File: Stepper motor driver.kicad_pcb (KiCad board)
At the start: 2 copper layers, 35.8 x 35.8 mm, 17 parts, among them P1 CONN_01X04, P2 CONN_01X03, P3 CONN_01X03, Q1 TIP120, Q2 TIP120, Q3 TIP120, Q4 TIP120, U1 74LS175, U2 74LS157

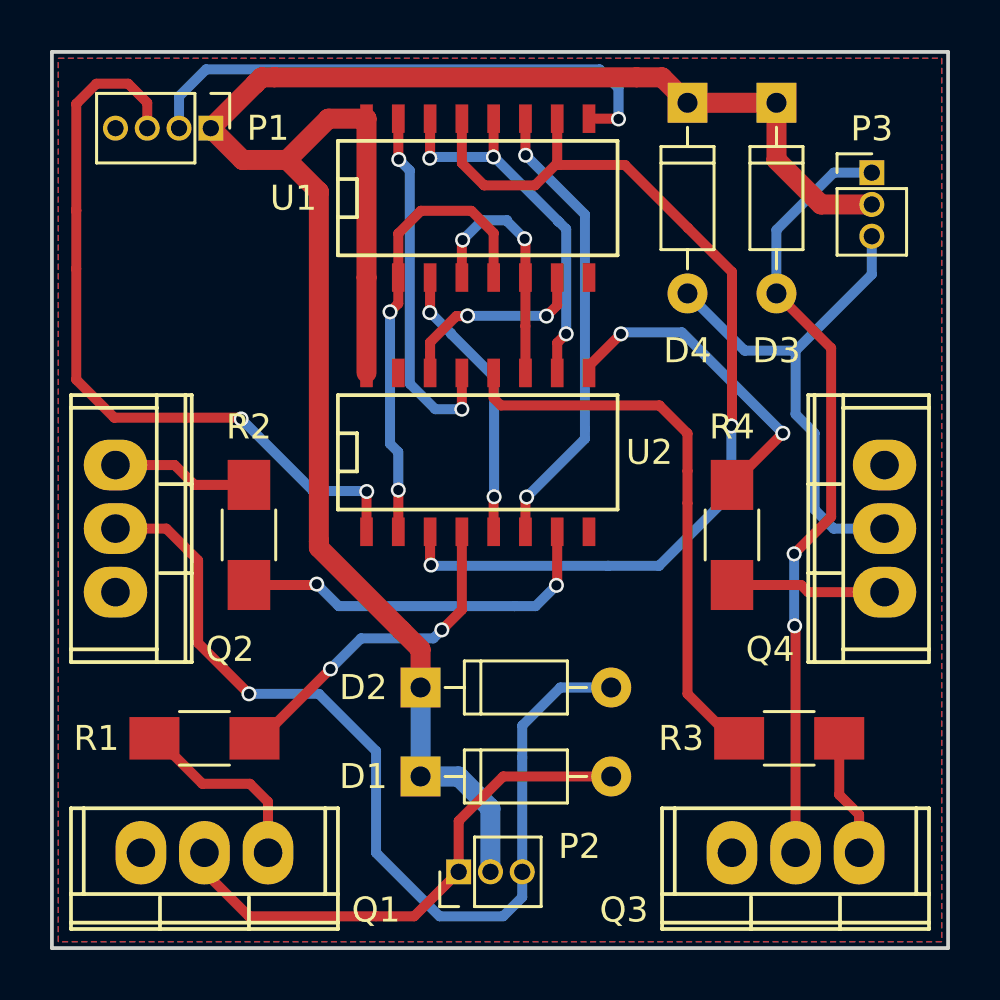
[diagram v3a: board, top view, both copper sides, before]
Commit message: Finished final trace routing
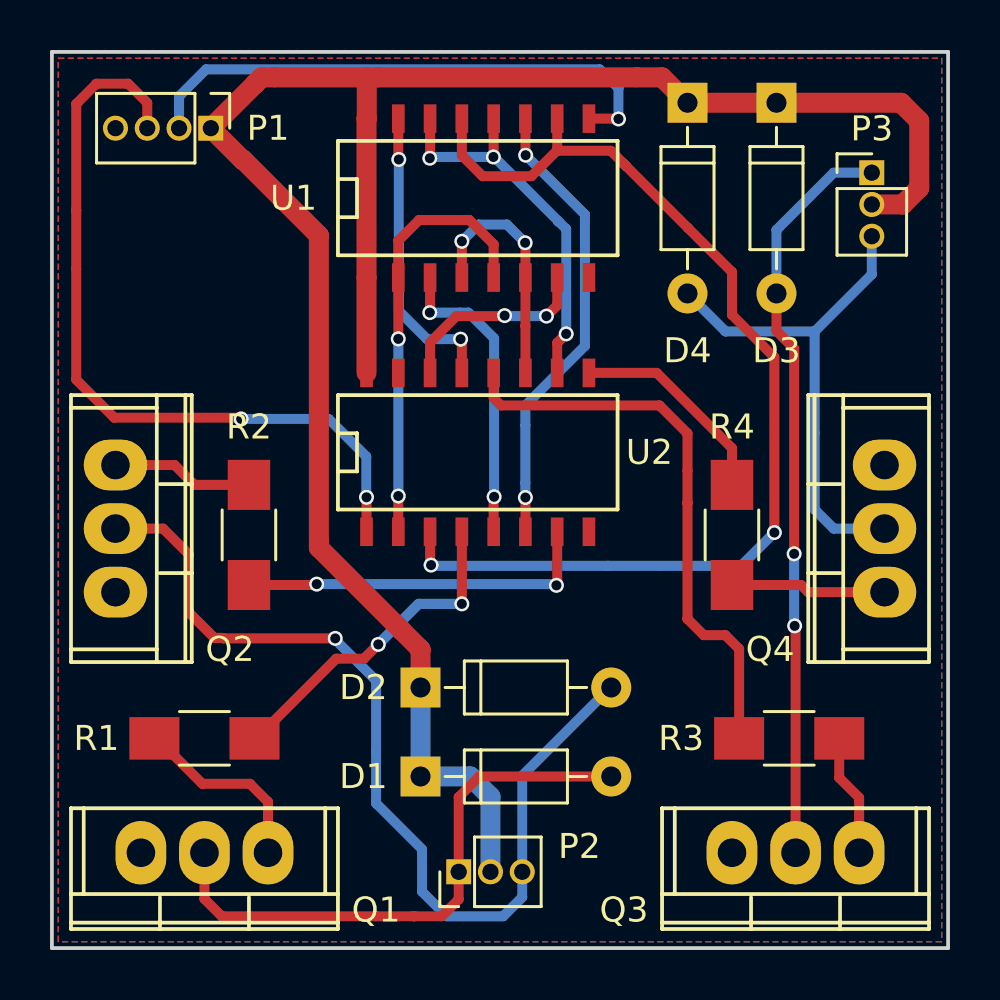
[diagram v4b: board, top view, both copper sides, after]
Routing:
- net Net-(R4-Pad2): track 13.2 -> 8.74 mm, vias 2 -> 0
- net Net-(R1-Pad2): track 13.6 -> 17.8 mm
- net /A2-: track 40.3 -> 43.1 mm
- net /B2+: track 14.7 -> 12.0 mm
- net /Coil1+: track 21.3 -> 23.9 mm
- net /Coil2+: track 31.2 -> 30.0 mm
- net VCC: track 81.0 -> 82.1 mm
- net /B1+: track 18.5 -> 17.5 mm
- net /B1-: track 11.2 -> 12.2 mm
- net /DIR: track 30.6 -> 31.4 mm
- net Net-(R2-Pad2): track 15.2 -> 14.5 mm
- net Net-(R3-Pad2): track 22.6 -> 23.2 mm
